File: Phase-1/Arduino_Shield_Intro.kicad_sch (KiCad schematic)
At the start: 30 parts, among them J1 Power, J2 Digital/PWM, J3 Analog, J4 Digital/PWM, J5 Flexor Digitorum Superficialis, J6 Flexor Carpi Radialis, U1 LM358, U2 LM358, U3 LM358

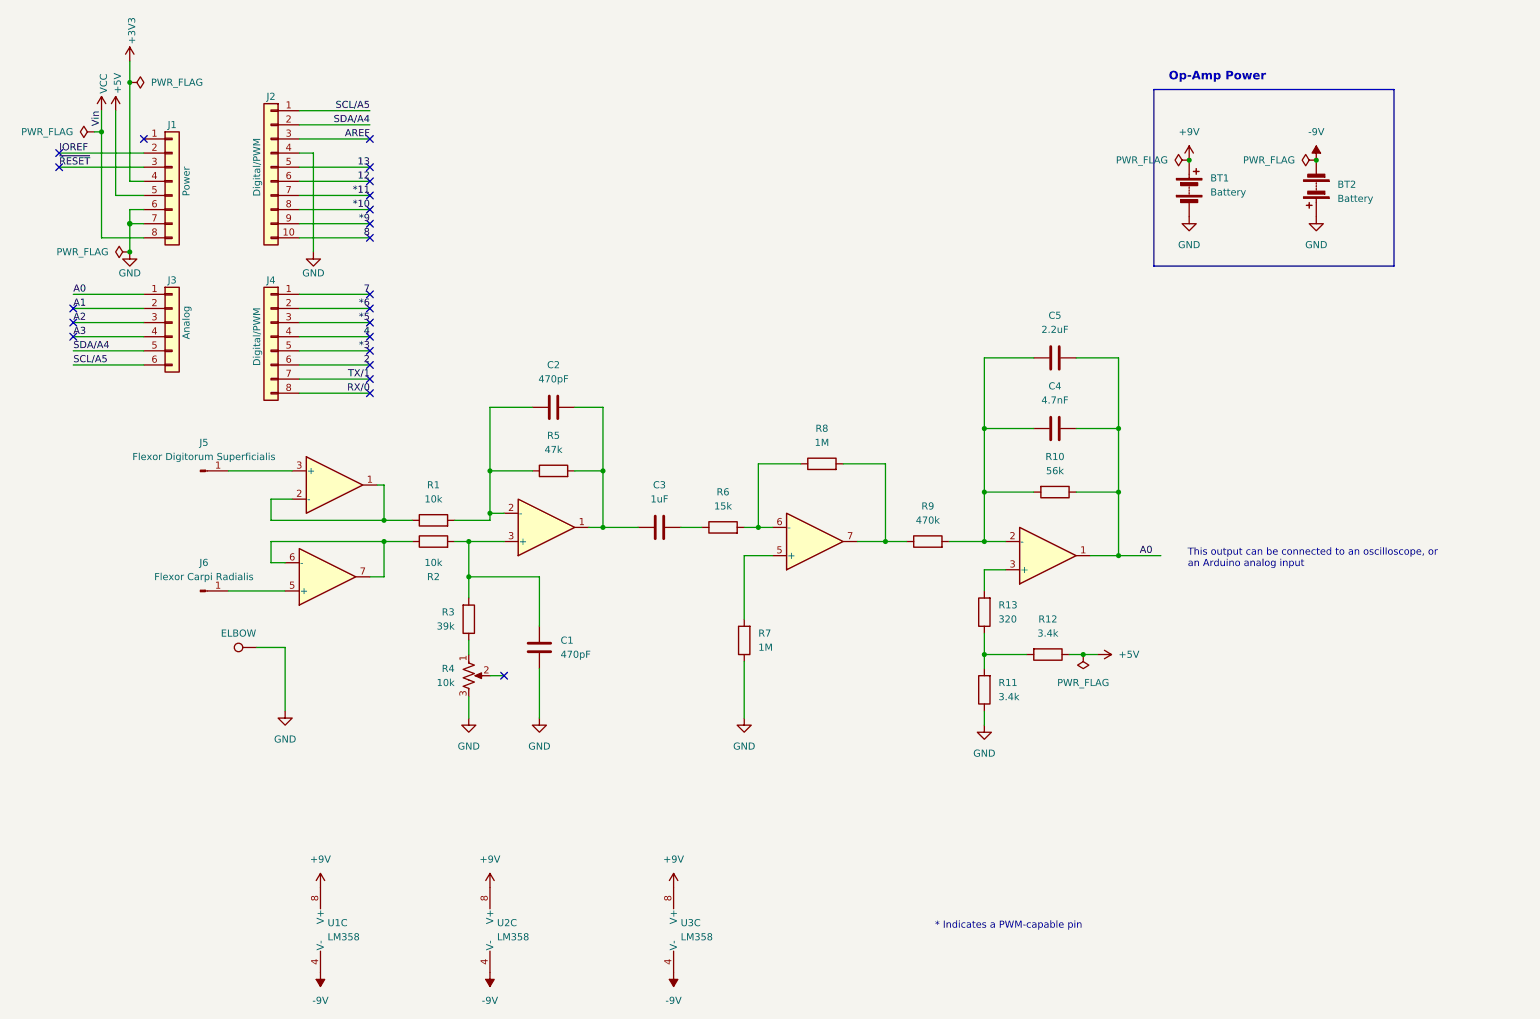
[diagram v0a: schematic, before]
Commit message: PCB for Phase 0
Made a PCB for Phase 0 bridge device.
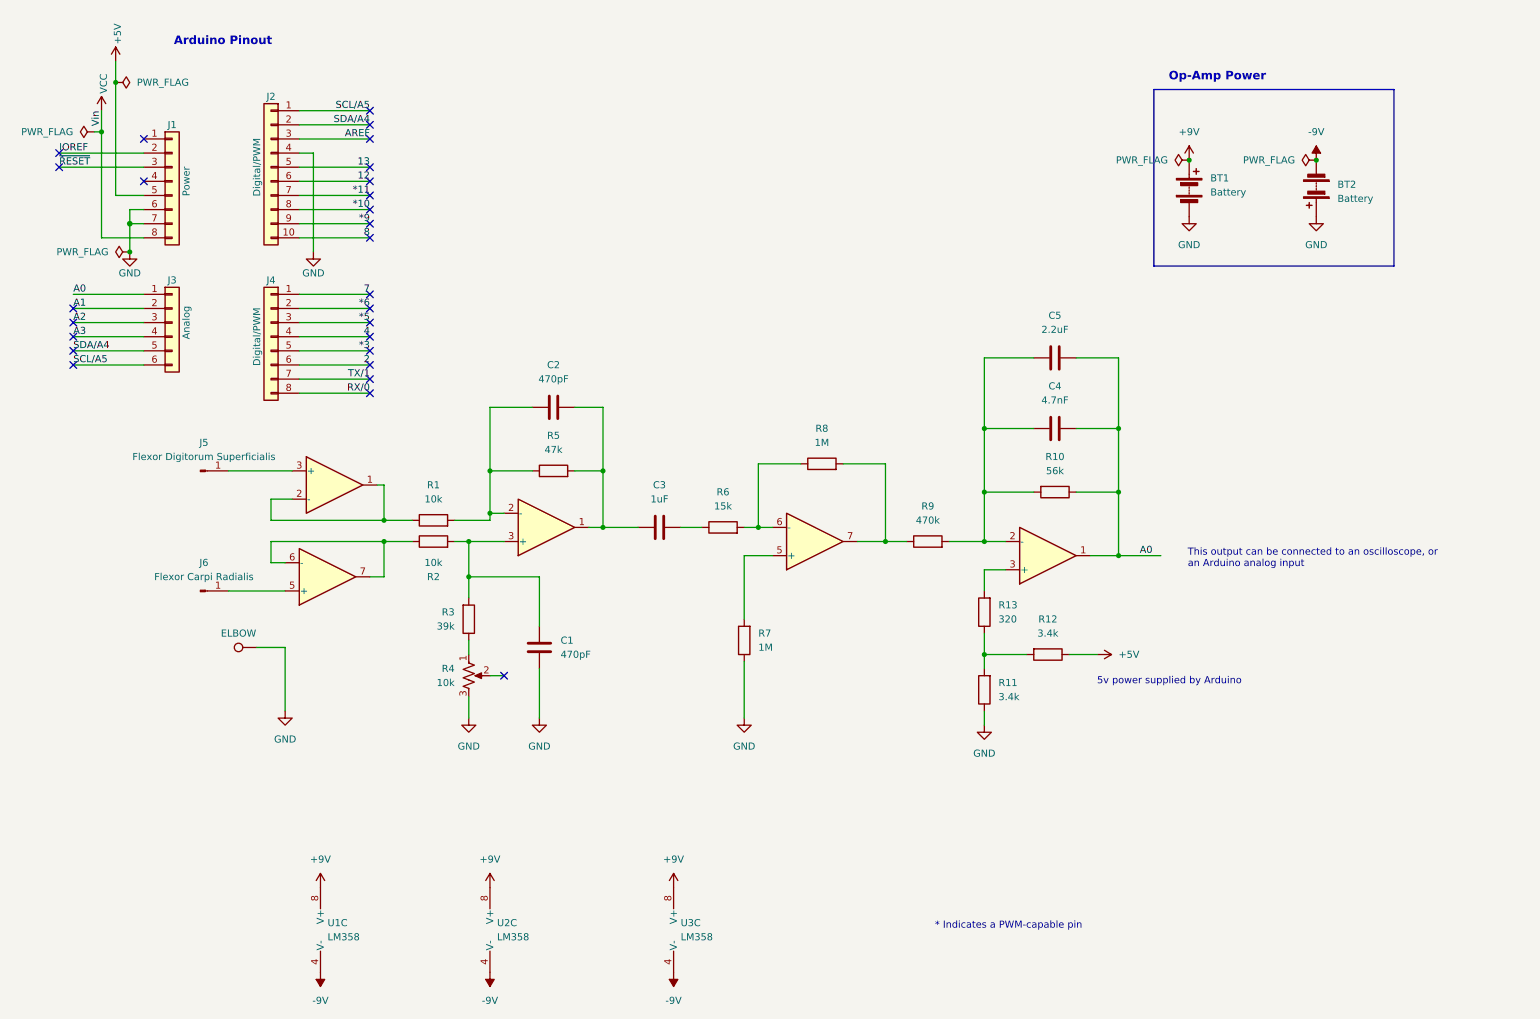
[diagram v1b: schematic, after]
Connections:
- net +3V3: no longer names the net of J1.4 (Pin_4)
- no-connect marks 22 -> 27
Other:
- note added: "5v power supplied by Arduino"
- note added: "Arduino Pinout"
